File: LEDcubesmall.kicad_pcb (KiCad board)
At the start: 4 copper layers, 10.5 x 10.5 mm, 22 parts, among them J1 Conn_01x03, J2 Conn_01x03, J3 Conn_01x03, J4 Conn_01x03

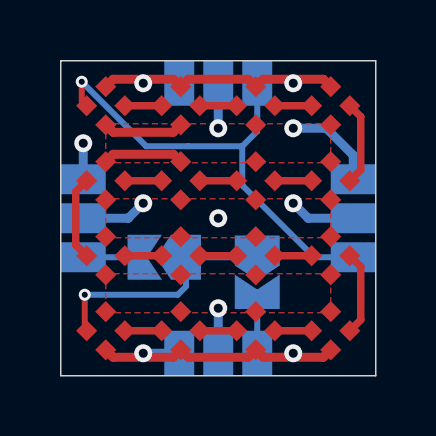
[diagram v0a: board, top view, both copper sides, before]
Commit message: corners, add missing gnd connection
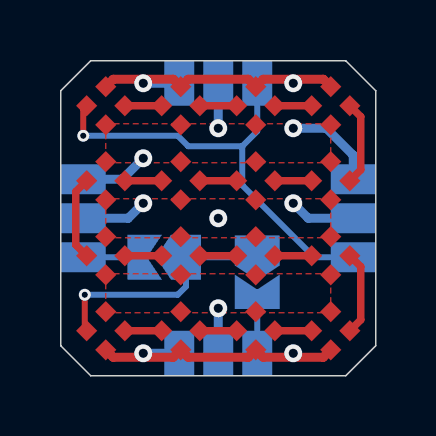
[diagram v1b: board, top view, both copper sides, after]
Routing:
- net +5V: track 12.8 -> 7.41 mm
- net GND: track 21.8 -> 24.1 mm
- net /DIN: track 15.4 -> 14.8 mm
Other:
- outline, holes or cut-outs redrawn
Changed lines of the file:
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@@
   (general
     (thickness 0.8)
-    (drawings 16)
-    (tracks 87)
+    (drawings 20)
+    (tracks 83)
     (zones 0)
     (modules 22)
@@
     )
   )
+  (gr_line (start -0.5 -1.5) (end 8 -1.5) (layer Edge.Cuts) (width 0.05))
+  (gr_line (start -1.5 8) (end -1.5 -0.5) (layer Edge.Cuts) (width 0.05))
+  (gr_line (start 8 9) (end -0.5 9) (layer Edge.Cuts) (width 0.05))
+  (gr_line (start 9 -0.5) (end 9 8) (layer Edge.Cuts) (width 0.05))
+  (gr_line (start -0.5 -1.5) (end -1.5 -0.5) (layer Edge.Cuts) (width 0.05))
+  (gr_line (start 8 9) (end 9 8) (layer Edge.Cuts) (width 0.05))
+  (gr_line (start -1.5 8) (end -0.5 9) (layer Edge.Cuts) (width 0.05))
+  (gr_line (start 8 -1.5) (end 9 -0.5) (layer Edge.Cuts) (width 0.05))
   (gr_line (start 1.65 7.2) (end 3 7.2) (layer B.SilkS) (width 0.12))
   (gr_line (start 1.65 8.95) (end 1.65 7.2) (layer B.SilkS) (width 0.12))
@@
   (gr_poly (pts (xy 7.15 4.5) (xy 7.15 5.6) (xy 6.4 5.05)) (layer B.SilkS) (width 0.1))
   (gr_poly (pts (xy 4.5 0.35) (xy 5.6 0.35) (xy 5.05 1.1)) (layer B.SilkS) (width 0.1))
-  (gr_line (start -1.5 9) (end -1.5 -1.5) (layer Edge.Cuts) (width 0.05))
-  (gr_line (start 9 9) (end -1.5 9) (layer Edge.Cuts) (width 0.05))
-  (gr_line (start 9 -1.5) (end 9 9) (layer Edge.Cuts) (width 0.05))
-  (gr_line (start -1.5 -1.5) (end 9 -1.5) (layer Edge.Cuts) (width 0.05))
   (segment (start 2.252514 -0.883882) (end 0.247486 -0.883882) (width 0.3) (layer F.Cu) (net 1))
   (via (at 1.25 -0.75) (size 0.6) (drill 0.3) (layers F.Cu B.Cu) (net 1))
-  (segment (start 2.5 -0.636396) (end 2.252514 -0.883882) (width 0.3) (layer F.Cu) (net 1))
-  (segment (start 0.247486 -0.883882) (end 0 -0.636396) (width 0.3) (layer F.Cu) (net 1))
+  (segment (start 2.5 -0.636396) (end 2.252514 -0.883882) (width 0.3) (layer F.Cu) (net 1) (status 10))
+  (segment (start 0.247486 -0.883882) (end 0 -0.636396) (width 0.3) (layer F.Cu) (net 1) (status 20))
   (segment (start 7.252514 -0.883882) (end 5.247486 -0.883882) (width 0.3) (layer F.Cu) (net 1))
   (via (at 6.25 -0.75) (size 0.6) (drill 0.3) (layers F.Cu B.Cu) (net 1))
-  (segment (start 7.5 -0.636396) (end 7.252514 -0.883882) (width 0.3) (layer F.Cu) (net 1))
-  (segment (start 5.247486 -0.883882) (end 5 -0.636396) (width 0.3) (layer F.Cu) (net 1))
+  (segment (start 7.5 -0.636396) (end 7.252514 -0.883882) (width 0.3) (layer F.Cu) (net 1) (status 10))
+  (segment (start 5.247486 -0.883882) (end 5 -0.636396) (width 0.3) (layer F.Cu) (net 1) (status 20))
   (segment (start 5.247486 8.383882) (end 7.252514 8.383882) (width 0.3) (layer F.Cu) (net 1))
   (via (at 6.25 8.25) (size 0.6) (drill 0.3) (layers F.Cu B.Cu) (net 1))
-  (segment (start 5 8.136396) (end 5.247486 8.383882) (width 0.3) (layer F.Cu) (net 1))
-  (segment (start 7.252514 8.383882) (end 7.5 8.136396) (width 0.3) (layer F.Cu) (net 1))
-  (segment (start -0.75 3.75) (end 0.75 3.75) (width 0.3) (layer B.Cu) (net 2))
-  (via (at -0.75 1.25) (size 0.6) (drill 0.3) (layers F.Cu B.Cu) (net 1))
-  (segment (start -0.75 2.45) (end -0.75 1.25) (width 0.3) (layer B.Cu) (net 1) (status 10))
+  (segment (start 5 8.136396) (end 5.247486 8.383882) (width 0.3) (layer F.Cu) (net 1) (status 10))
+  (segment (start 7.252514 8.383882) (end 7.5 8.136396) (width 0.3) (layer F.Cu) (net 1) (status 20))
   (via (at 1.25 8.25) (size 0.6) (drill 0.3) (layers F.Cu B.Cu) (net 1))
   (segment (start 2.45 8.25) (end 1.25 8.25) (width 0.3) (layer B.Cu) (net 1) (status 10))
@@
   (segment (start 2.5 -0.636396) (end 2.747486 -0.883882) (width 0.3) (layer F.Cu) (net 1) (status 10))
   (segment (start 0.247486 8.383882) (end 2.252514 8.383882) (width 0.3) (layer F.Cu) (net 1))
-  (segment (start 2.252514 8.383882) (end 2.5 8.136396) (width 0.3) (layer F.Cu) (net 1))
-  (segment (start 0 8.136396) (end 0.247486 8.383882) (width 0.3) (layer F.Cu) (net 1))
-  (segment (start 4.752514 8.383882) (end 5 8.136396) (width 0.3) (layer F.Cu) (net 1))
+  (segment (start 2.252514 8.383882) (end 2.5 8.136396) (width 0.3) (layer F.Cu) (net 1) (status 20))
+  (segment (start 0 8.136396) (end 0.247486 8.383882) (width 0.3) (layer F.Cu) (net 1) (status 10))
+  (segment (start 4.752514 8.383882) (end 5 8.136396) (width 0.3) (layer F.Cu) (net 1) (status 20))
   (segment (start 2.747486 8.383882) (end 4.752514 8.383882) (width 0.3) (layer F.Cu) (net 1))
-  (segment (start 2.5 8.136396) (end 2.747486 8.383882) (width 0.3) (layer F.Cu) (net 1))
+  (segment (start 2.5 8.136396) (end 2.747486 8.383882) (width 0.3) (layer F.Cu) (net 1) (status 10))
   (via (at 3.75 3.75) (size 0.6) (drill 0.3) (layers F.Cu B.Cu) (net 1))
   (segment (start 8.25 1.65) (end 7.35 0.75) (width 0.3) (layer B.Cu) (net 1))
-  (segment (start 8.25 2.45) (end 8.25 1.65) (width 0.3) (layer B.Cu) (net 1))
+  (segment (start 8.25 2.45) (end 8.25 1.65) (width 0.3) (layer B.Cu) (net 1) (status 10))
   (via (at 6.25 0.75) (size 0.6) (drill 0.3) (layers F.Cu B.Cu) (net 1))
   (segment (start 7.35 0.75) (end 6.25 0.75) (width 0.3) (layer B.Cu) (net 1))
+  (via (at 1.25 1.75) (size 0.6) (drill 0.3) (layers F.Cu B.Cu) (net 1))
+  (segment (start -0.75 2.45) (end 0.55 2.45) (width 0.3) (layer B.Cu) (net 1) (status 10))
+  (segment (start 0.55 2.45) (end 1.25 1.75) (width 0.3) (layer B.Cu) (net 1))
+  (segment (start 1.25 -0.75) (end 2.45 -0.75) (width 0.3) (layer B.Cu) (net 1))
+  (segment (start -0.75 3.75) (end 0.75 3.75) (width 0.3) (layer B.Cu) (net 2) (status 10))
   (segment (start 3.75 -0.75) (end 3.75 0.75) (width 0.3) (layer B.Cu) (net 2) (status 10))
   (via (at 3.75 0.75) (size 0.6) (drill 0.3) (layers F.Cu B.Cu) (net 2))
-  (segment (start 0.247486 0.883882) (end 2.252514 0.883882) (width 0.3) (layer F.Cu) (net 2))
-  (segment (start 2.252514 0.883882) (end 2.5 0.636396) (width 0.3) (layer F.Cu) (net 2))
-  (segment (start 0 0.636396) (end 0.247486 0.883882) (width 0.3) (layer F.Cu) (net 2))
-  (segment (start 2.252514 1.616118) (end 2.5 1.863604) (width 0.3) (layer F.Cu) (net 2))
-  (segment (start 0.247486 1.616118) (end 2.252514 1.616118) (width 0.3) (layer F.Cu) (net 2))
-  (segment (start 0 1.863604) (end 0.247486 1.616118) (width 0.3) (layer F.Cu) (net 2))
-  (segment (start 8.25 3.75) (end 6.75 3.75) (width 0.3) (layer B.Cu) (net 2))
+  (segment (start 8.25 3.75) (end 6.75 3.75) (width 0.3) (layer B.Cu) (net 2) (status 10))
   (via (at 6.25 3.25) (size 0.6) (drill 0.3) (layers F.Cu B.Cu) (net 2))
   (segment (start 6.75 3.75) (end 6.25 3.25) (width 0.3) (layer B.Cu) (net 2))
@@
   (segment (start 3.136396 7.5) (end 4.363604 7.5) (width 0.25) (layer F.Cu) (net 16) (status 30))
   (segment (start 0.636396 7.5) (end 1.863604 7.5) (width 0.25) (layer F.Cu) (net 17) (status 30))
-  (segment (start 5.05 -0.75) (end 5.05 0.85) (width 0.2) (layer B.Cu) (net 18))
-  (segment (start 4.549999 1.350001) (end 2.750001 1.350001) (width 0.2) (layer B.Cu) (net 18))
+  (segment (start 5.05 -0.75) (end 5.05 0.85) (width 0.2) (layer B.Cu) (net 18) (status 10))
   (segment (start 5.05 0.85) (end 4.549999 1.350001) (width 0.2) (layer B.Cu) (net 18))
-  (via (at -0.8 -0.8) (size 0.4) (drill 0.2) (layers F.Cu B.Cu) (net 18))
-  (segment (start 2.750001 1.350001) (end 1.350001 1.350001) (width 0.2) (layer B.Cu) (net 18))
-  (segment (start 1.350001 1.350001) (end -0.8 -0.8) (width 0.2) (layer B.Cu) (net 18))
-  (segment (start -0.8 -0.163604) (end -0.636396 0) (width 0.2) (layer F.Cu) (net 18))
-  (segment (start -0.8 -0.8) (end -0.8 -0.163604) (width 0.2) (layer F.Cu) (net 18))
   (segment (start 4.549999 2.650719) (end 4.549999 1.350001) (width 0.2) (layer B.Cu) (net 18))
-  (segment (start 8.25 5.05) (end 6.94928 5.05) (width 0.2) (layer B.Cu) (net 18))
+  (segment (start 8.25 5.05) (end 6.94928 5.05) (width 0.2) (layer B.Cu) (net 18) (status 10))
   (segment (start 6.94928 5.05) (end 4.549999 2.650719) (width 0.2) (layer B.Cu) (net 18))
+  (via (at -0.75 1) (size 0.4) (drill 0.2) (layers F.Cu B.Cu) (net 18))
+  (segment (start -0.75 1) (end 2.4 1) (width 0.2) (layer B.Cu) (net 18))
+  (segment (start 2.750001 1.350001) (end 4.549999 1.350001) (width 0.2) (layer B.Cu) (net 18))
+  (segment (start 2.4 1) (end 2.750001 1.350001) (width 0.2) (layer B.Cu) (net 18))
+  (segment (start -0.75 0.113604) (end -0.636396 0) (width 0.2) (layer F.Cu) (net 18) (status 30))
+  (segment (start -0.75 1) (end -0.75 0.113604) (width 0.2) (layer F.Cu) (net 18) (status 20))
   (segment (start 2.675 5.05) (end 4.825 5.05) (width 0.2) (layer B.Cu) (net 19) (status 30))
   (via (at -0.7 6.3) (size 0.4) (drill 0.2) (layers F.Cu B.Cu) (net 19))
